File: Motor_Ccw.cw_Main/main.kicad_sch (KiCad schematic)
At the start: 67 parts, among them J1 KF128-3.81-3P, J2 KF128-3.81-2P, J3 Conn_01x04, J5 KF128-3.81-2P, J8 Conn_01x04, SW1 6x6x5mm, SW2 6x6x5mm, U1 STM32F030C8T6, U13 LMV358TP-SR, U2 XL1509-5.0E1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

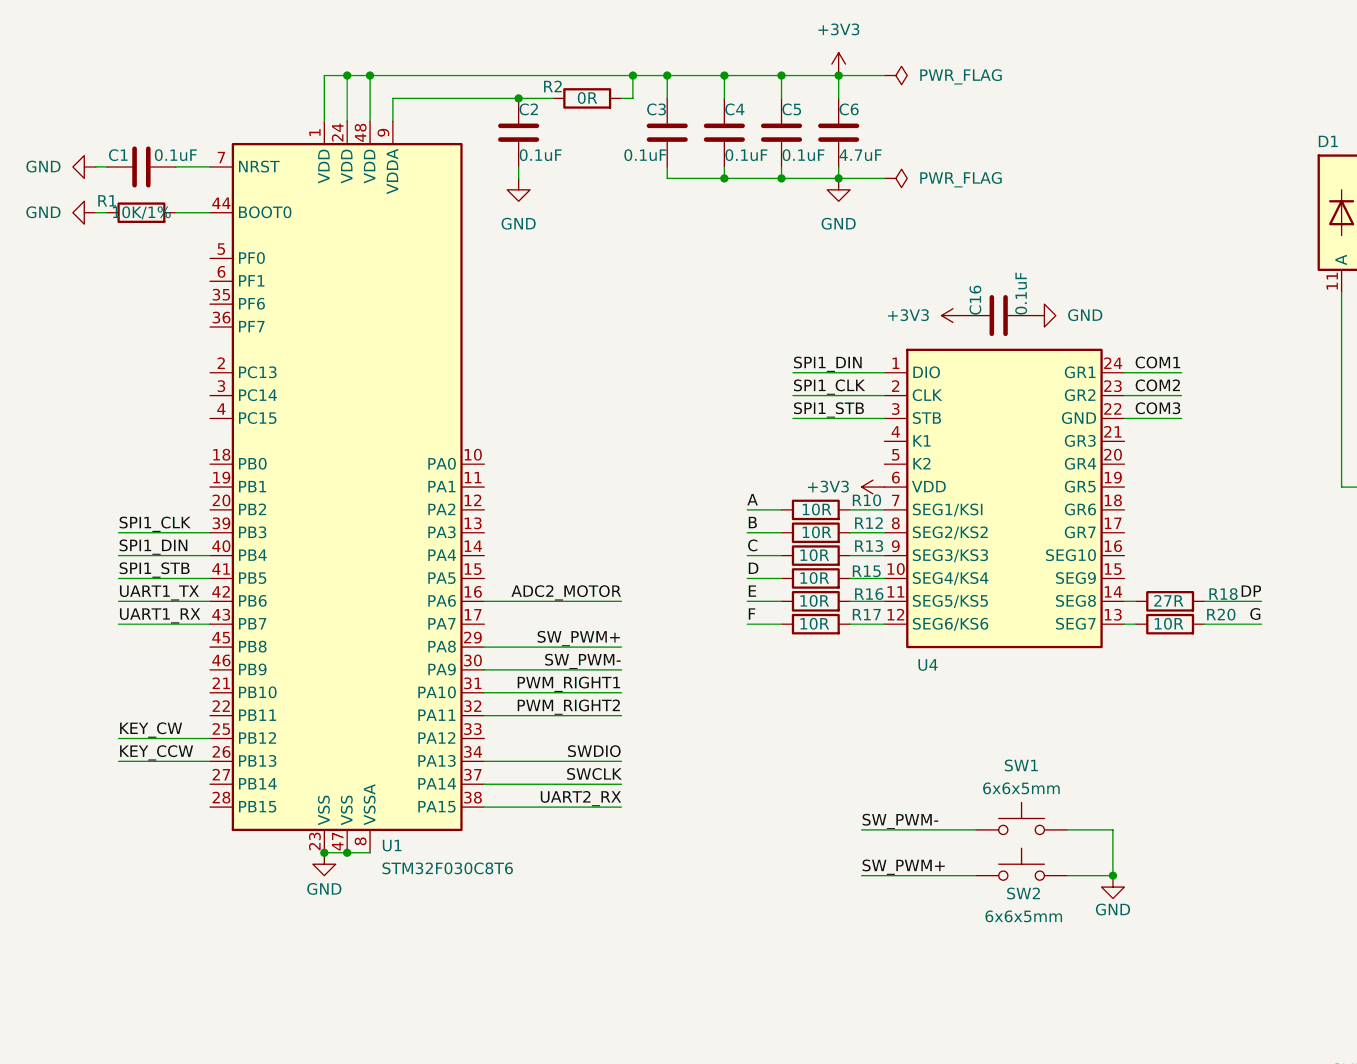
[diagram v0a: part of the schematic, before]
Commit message: 修改封装，修改原理图
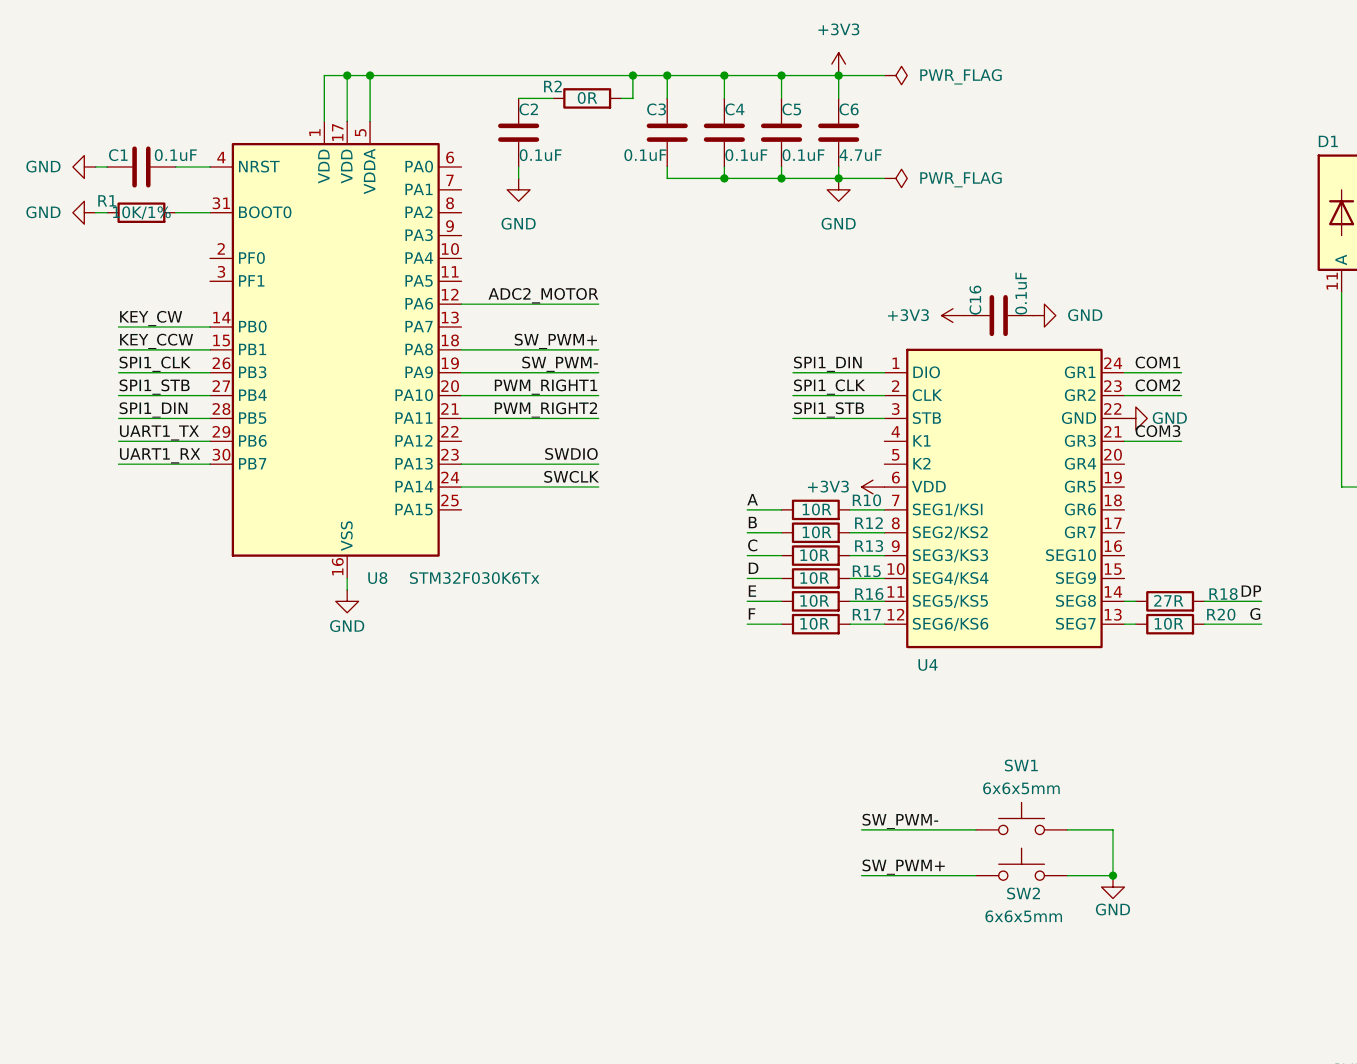
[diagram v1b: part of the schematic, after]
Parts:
- removed U1: STM32F030C8T6, Package_QFP:LQFP-48_7x7mm_P0.5mm, symbol MCU_ST_STM32F0:STM32F030C8Tx
- added U8: STM32F030K6Tx, Package_QFP:LQFP-32_7x7mm_P0.8mm, symbol MCU_ST_STM32F0:STM32F030K6Tx
- J1: footprint TerminalBlock_MetzConnect:TerminalBlock_MetzConnect_Type086_RT03403HBLC_1x03_P3.81mm_Horizontal -> Ovo_TerminalBlock_MetzConnect:TerminalBlock_MetzConnect_Type086_RT03403HBLC_1x03_P3.81mm_Horizontal
- J2, J5: footprint TerminalBlock_MetzConnect:TerminalBlock_MetzConnect_Type086_RT03402HBLC_1x02_P3.81mm_Horizontal -> Ovo_TerminalBlock_MetzConnect:TerminalBlock_MetzConnect_Type086_RT03402HBLC_1x02_P3.81mm_Horizontal
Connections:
- net +3V3: now also U8.1 (VDD), U8.17 (VDD), U8.5 (VDDA)
- net ADC2_MOTOR: now also U8.12 (PA6)
- net COM3: now also U4.21 (GR3); no longer U4.22 (GND)
- net GND: now also U4.22 (GND), U8.16 (VSS), U8.32 (VSS)
- net KEY_CCW: now also U8.15 (PB1)
- net KEY_CW: now also U8.14 (PB0)
- net PWM_RIGHT1: now also U8.20 (PA10)
- net PWM_RIGHT2: now also U8.21 (PA11)
- net SPI1_CLK: now also U8.26 (PB3)
- net SPI1_DIN: now also U8.28 (PB5)
- net SPI1_STB: now also U8.27 (PB4)
- net SWCLK: now also U8.24 (PA14)
- net SWDIO: now also U8.23 (PA13)
- net SW_PWM+: now also U8.18 (PA8)
- net SW_PWM-: now also U8.19 (PA9)
- net UART1_RX: now also U8.30 (PB7)
- net UART1_TX: now also U8.29 (PB6)
- net at C1.2: now also U8.4 (NRST)
- net at R1.2: now also U8.31 (BOOT0)
